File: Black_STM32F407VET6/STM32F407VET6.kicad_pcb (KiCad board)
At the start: 2 copper layers, 81.3 x 99.7 mm, 103 parts, among them J1 T0, J10 Fan2, J11 Fan1, J12 X_logic, J13 Microsteps, J14 X-, J15 Y-, J16 Z-, J17 Left, J18 Y_logic, J19 X+, J2 T1, J20 Y+, J21 Z+, J22 Microsteps, J23 EXP2, J24 Z_logic, J25 Bottom, J26 Microsteps, J27 EXP1, J28 E0_logic, J29 Microsteps, J3 TB, J30 Right, J31 E1_logic, J32 Microsteps, J33 X_motor, J34 Y_motor, J35 Z_motor, J36 E0_motor, J37 E1_motor, J38 X, J39 Y, J4 TC, J40 Z, J41 E0, J42 E1, J43 Fan0, J44 COM, J45 USB, J47 I2C, J48 SPI, J49 SPI, J5 + VIN -, J50 SDIO, J51 Servo, J52 Servo, J53 PowerSelect, J54 Power, J55 PD11, J56 Power, J6 - HotBed +, J7 Heater0, J8 Heater1, J9 Fan3, Q1 Q_NMOS_GDS, Q2 Q_NMOS_GDS, Q3 Q_NMOS_GDS, Q4 Q_NMOS_GSD, Q5 Q_NMOS_GSD, Q6 Q_NMOS_GSD, Q7 Q_NMOS_GSD, U1 SN74AHC, U2 SN74AHC, U3 SN74AHC, U4 LM2596S-5, U5 AT24CS01-SSHM

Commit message: Changed parts in schematic to be cheaper, PCB changed to be DIY friendly
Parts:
- removed REF**: OSHW-Symbol_6.7x6mm_SilkScreen, Symbol:OSHW-Symbol_6.7x6mm_SilkScreen
- removed U1, U2, U3: SN74AHC, Package_TO_SOT_SMD:SOT-23-5
- added Q10: BCX70, Package_TO_SOT_SMD:SOT-23, F.Cu at (217.6, 379.5)
- added Q11: BCX70, Package_TO_SOT_SMD:SOT-23, F.Cu at (214.1, 384.3)
- added Q12: IRLR8726PBF, Package_TO_SOT_SMD:TO-252-2, F.Cu at (227.9, 334.9)
- added Q13: IRLR8726PBF, Package_TO_SOT_SMD:TO-252-2, F.Cu at (213.0, 347.5)
- added Q14: IRLR8726PBF, Package_TO_SOT_SMD:TO-252-2, F.Cu at (200.0, 359.8)
- added Q8: IRLML0030TRPBF, Package_TO_SOT_SMD:SOT-23, F.Cu at (223.9, 375.0)
- added Q9: BCX70, Package_TO_SOT_SMD:SOT-23, F.Cu at (219.5, 375.0)
- added R23: 100K, Resistor_SMD:R_0603_1608Metric, F.Cu at (251.8, 344.4)
- added R24: 100K, Resistor_SMD:R_0603_1608Metric, F.Cu at (256.2, 339.9)
- added R25: 100K, Resistor_SMD:R_0603_1608Metric, F.Cu at (189.4, 384.4)
- added R26: 10K, Resistor_SMD:R_0603_1608Metric, F.Cu at (237.3, 365.2)
- added R27: 10K, Resistor_SMD:R_0603_1608Metric, F.Cu at (228.1, 374.8)
- added R28: 10K, Resistor_SMD:R_0603_1608Metric, F.Cu at (253.6, 349.4)
- D1, R18, R19, R20, R21, R22: moved to F.Cu
- J1, J2, J3, J4: footprint Connector_JST:JST_XH_B02B-XH-A_1x02_P2.50mm_Vertical -> Connector_JST:JST_XH_B2B-XH-AM_1x02_P2.50mm_Vertical
- J10: value Fan2 -> - HotBed +; footprint Connector_JST:JST_XH_B02B-XH-A_1x02_P2.50mm_Vertical -> Connector_JST:JST_XH_B2B-XH-A_1x02_P2.50mm_Vertical
- J11: value Fan1 -> Heater0; footprint Connector_JST:JST_XH_B02B-XH-A_1x02_P2.50mm_Vertical -> Connector_JST:JST_XH_B2B-XH-A_1x02_P2.50mm_Vertical
- J14, J15, J16, J19, J20, J21: footprint Connector_JST:JST_XH_B03B-XH-A_1x03_P2.50mm_Vertical -> Connector_JST:JST_XH_B3B-XH-A_1x03_P2.50mm_Vertical
- J38, J39, J40, J41, J42: footprint Connector_JST:JST_XH_B04B-XH-A_1x04_P2.50mm_Vertical -> Connector_JST:JST_XH_B4B-XH-A_1x04_P2.50mm_Vertical
- J43: value Fan0 -> Heater1; footprint Connector_JST:JST_XH_B02B-XH-A_1x02_P2.50mm_Vertical -> Connector_JST:JST_XH_B2B-XH-AM_1x02_P2.50mm_Vertical
- J50: footprint Connector_JST:JST_XH_B09B-XH-A_1x09_P2.50mm_Vertical -> Connector_JST:JST_XH_B9B-XH-A_1x09_P2.50mm_Vertical
- J6: value - HotBed + -> Fan3; footprint TerminalBlock_MetzConnect:TerminalBlock_MetzConnect_Type055_RT01502HDWU_1x02_P5.00mm_Horizontal -> Connector_JST:JST_XH_B2B-XH-AM_1x02_P2.50mm_Vertical
- J7: value Heater0 -> Fan2; footprint TerminalBlock_MetzConnect:TerminalBlock_MetzConnect_Type059_RT06302HBWC_1x02_P3.50mm_Horizontal -> Connector_JST:JST_XH_B2B-XH-AM_1x02_P2.50mm_Vertical
- J8: value Heater1 -> Fan1; footprint TerminalBlock_MetzConnect:TerminalBlock_MetzConnect_Type059_RT06302HBWC_1x02_P3.50mm_Horizontal -> Connector_JST:JST_XH_B2B-XH-AM_1x02_P2.50mm_Vertical
- J9: value Fan3 -> Fan0; footprint Connector_JST:JST_XH_B02B-XH-A_1x02_P2.50mm_Vertical -> Connector_JST:JST_XH_B2B-XH-AM_1x02_P2.50mm_Vertical
- Q1, Q2, Q3: value Q_NMOS_GDS -> BCX70; footprint Package_TO_SOT_SMD:TO-252-2 -> Package_TO_SOT_SMD:SOT-23
- Q4, Q6, Q7: value Q_NMOS_GSD -> IRLML0030TRPBF
- Q5: value Q_NMOS_GSD -> BCX70
- R10, R12, R14: value 10 -> 100K
- R13: value 10K -> 100K
- R16: value 10 -> 10K
- moved J24 336.8 mm to (113.0, 398.3)
- moved J26 328.3 mm to (106.2, 400.8)
- moved C11 313.9 mm to (171.7, 380.5), turned to 0 degrees
- moved J27 312.5 mm to (155.2, 458.5), turned to 0 degrees
- moved R7 311.8 mm to (147.8, 385.4), turned to 0 degrees
- moved R6 311.7 mm to (143.7, 385.4), turned to 0 degrees
- moved J47 309.9 mm to (216.4, 402.3)
- moved J4 308.2 mm to (239.8, 393.2), turned to 0 degrees
- moved C7 307.1 mm to (171.7, 370.6), turned to 0 degrees
- moved R9 306.9 mm to (221.9, 378.5), turned to 0 degrees
- moved R8 304.0 mm to (228.1, 372.3), turned to 0 degrees
- moved R1 296.0 mm to (151.8, 385.4), turned to 0 degrees
- moved R2 295.2 mm to (162.5, 384.3), turned to 0 degrees
- moved C4 294.0 mm to (211.2, 378.7)
- moved J3 293.3 mm to (273.8, 361.7), turned to 0 degrees
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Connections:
- J10 pad 1: Net-(J10-Pad1) -> 12V
- J11 pad 1: Net-(J10-Pad1) -> 12V
- J43 pad 1: Net-(J10-Pad1) -> 12V
- J56 pad 2: Net-(J10-Pad1) -> GND
- J7 pad 1: Net-(J7-Pad1) -> 12V
- J7 pad 2: 12V -> Net-(J7-Pad2)
- J8 pad 1: Net-(J8-Pad1) -> 12V
- J8 pad 2: 12V -> Net-(J8-Pad2)
- J9 pad 1: Net-(J10-Pad1) -> 12V
- Q1 pad 1: Net-(Q1-Pad1) -> GND
- Q1 pad 2: Net-(J6-Pad2) -> Net-(Q1-Pad2)
- Q1 pad 3: GND -> Net-(Q1-Pad3)
- Q2 pad 1: Net-(Q2-Pad1) -> GND
- Q2 pad 2: Net-(J7-Pad1) -> Net-(Q2-Pad2)
- Q2 pad 3: GND -> Net-(Q2-Pad3)
- Q3 pad 1: Net-(Q3-Pad1) -> GND
- Q3 pad 2: Net-(J8-Pad1) -> Net-(Q3-Pad2)
- Q3 pad 3: GND -> Net-(Q3-Pad3)
- Q4 pad 1: Net-(Q4-Pad1) -> Net-(Q3-Pad3)
- Q4 pad 3: Net-(J9-Pad2) -> Net-(J8-Pad2)
- Q5 pad 1: Net-(Q5-Pad1) -> GND
- Q5 pad 2: GND -> Net-(Q5-Pad2)
- Q5 pad 3: Net-(J10-Pad2) -> Net-(Q5-Pad3)
- Q6 pad 1: Net-(Q6-Pad1) -> Net-(Q1-Pad3)
- Q6 pad 3: Net-(J11-Pad2) -> Net-(J6-Pad2)
- Q7 pad 1: Net-(Q7-Pad1) -> Net-(Q2-Pad3)
- Q7 pad 3: Net-(J43-Pad2) -> Net-(J7-Pad2)
- R10 pad 1: Net-(Q4-Pad1) -> Fan3
- R10 pad 2: Fan3 -> Net-(Q1-Pad2)
- R11 pad 1: GND -> Net-(Q3-Pad3)
- R11 pad 2: Net-(Q4-Pad1) -> 12V
- R12 pad 1: Net-(Q5-Pad1) -> Fan2
- R12 pad 2: Fan2 -> Net-(Q2-Pad2)
- R13 pad 1: GND -> Fan1
- R13 pad 2: Net-(Q5-Pad1) -> Net-(Q3-Pad2)
- R14 pad 1: Net-(Q6-Pad1) -> Fan0
- R14 pad 2: Fan1 -> Net-(Q5-Pad2)
- R15 pad 1: GND -> Net-(Q1-Pad3)
- R15 pad 2: Net-(Q6-Pad1) -> 12V
- R16 pad 1: Net-(Q7-Pad1) -> Net-(Q2-Pad3)
- R16 pad 2: Fan0 -> 12V
- R17 pad 1: GND -> Net-(Q5-Pad3)
- R17 pad 2: Net-(Q7-Pad1) -> 12V
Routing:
- net GND: track 756.5 -> 0.00 mm, vias 104 -> 0
- net 5V: track 268.4 -> 0.00 mm, vias 1 -> 0
- net 3V3: track 325.5 -> 66.4 mm, vias 5 -> 0
- net 12V: track 304.2 -> 73.4 mm, vias 5 -> 0
- net Z_En: track 79.3 -> 0.00 mm, vias 1 -> 0
- net X_En: track 69.6 -> 0.00 mm
- net Y-: track 67.5 -> 0.00 mm
- net Heater0: track 63.9 -> 0.00 mm
- net Z_Step: track 62.3 -> 0.00 mm
- net Z_Dir: track 62.3 -> 0.00 mm
- net E0_En: track 57.1 -> 0.00 mm
- net Heater1: track 53.7 -> 0.00 mm
- net Y_En: track 53.0 -> 0.00 mm, vias 1 -> 0
- net E1_En: track 51.2 -> 0.00 mm, vias 1 -> 0
- net Y+: track 51.1 -> 0.00 mm
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- removed copper zone on B.Cu, net GND
- removed copper zone on F.Cu, net GND
- removed copper zone on B.Cu, net Net-(J6-Pad2)
- removed copper zone on B.Cu, net Net-(J7-Pad1)
- removed copper zone on B.Cu, net Net-(J8-Pad1)
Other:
- board outline removed
- rule pad_to_mask_clearance: 0.051 -> 0
- board text removed: "3V3"
- board text removed: "5V"
- board text removed: "CLK"
- board text removed: "CMD"
- board text removed: "CS"
- board text removed: "CS1"
- board text removed: "CS2"
- board text removed: "D0"
- board text removed: "D1"
- board text removed: "D2"
- board text removed: "D3"
- board text removed: "DM"
- board text removed: "DP"
- board text removed: "Gnd"
- board text removed: "MISO"
- board text removed: "MOSI"
- board text removed: "PWM"
- board text removed: "Rx"
- board text removed: "SCK"
- board text removed: "SCL"
- board text removed: "SDA"
- board text removed: "SDDET"
- board text removed: "T0"
- board text removed: "T1"
- board text removed: "TB"
- board text removed: "TC"
- board text removed: "Tx"
- board text removed: "VIN"
- board text removed: "Vcc"
- board text removed: "X+"
- board text removed: "X-"
- board text removed: "Y+"
- board text removed: "Y-"
- board text removed: "Z+"
- board text removed: "Z-"
- board text removed: "https://github.com/jmz52/hardware"

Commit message: Arranged parts on PCB, swapped a few pins in schematic to align connectors.
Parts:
- removed C11: 100uF 35V, Capacitor_SMD:CP_Elec_8x6.9
- removed C5: 100uF 35V, Capacitor_THT:CP_Radial_D8.0mm_P3.50mm
- removed C6: 220uF 35V, Capacitor_THT:CP_Radial_D6.3mm_P2.50mm
- removed D1: SS14, Diode_SMD:D_SMA
- removed J21: Z+, Connector_JST:JST_XH_B3B-XH-A_1x03_P2.50mm_Vertical
- removed J31: E1_logic, Connector_PinSocket_2.54mm:PinSocket_1x08_P2.54mm_Vertical
- removed J32: Microsteps, Connector_PinHeader_2.54mm:PinHeader_2x03_P2.54mm_Vertical
- removed J35: Z_motor, Connector_PinSocket_2.54mm:PinSocket_1x08_P2.54mm_Vertical
- removed J37: E1_motor, Connector_PinSocket_2.54mm:PinSocket_1x08_P2.54mm_Vertical
- removed J40: Z, Connector_JST:JST_XH_B4B-XH-A_1x04_P2.50mm_Vertical
- removed J42: E1, Connector_JST:JST_XH_B4B-XH-A_1x04_P2.50mm_Vertical
- removed J45: USB, Connector_PinHeader_2.54mm:PinHeader_1x04_P2.54mm_Vertical
- removed L1: 47uH, Inductor_THT:L_Radial_D9.5mm_P5.00mm_Fastron_07HVP
- removed R6, R7, R8, R9: 4K7, Resistor_SMD:R_0603_1608Metric
- removed U4: LM2596S-5, Package_TO_SOT_SMD:TO-263-5_TabPin3
- added JXXX1: ESC_POWER, TerminalBlock_MetzConnect:TerminalBlock_MetzConnect_Type055_RT01502HDWU_1x02_P5.00mm_Horizontal, F.Cu at (144.8, 118.7)
- J12: value X_logic -> X-; footprint Connector_PinSocket_2.54mm:PinSocket_1x08_P2.54mm_Vertical -> Connector_JST:JST_XH_B3B-XH-A_1x03_P2.50mm_Vertical
- J13: value Microsteps -> Y-; footprint Connector_PinHeader_2.54mm:PinHeader_2x03_P2.54mm_Vertical -> Connector_JST:JST_XH_B3B-XH-A_1x03_P2.50mm_Vertical
- J14: value X- -> Z-
- J15: value Y- -> Z+
- J16: value Z- -> USB_B; footprint Connector_JST:JST_XH_B3B-XH-A_1x03_P2.50mm_Vertical -> Connector_USB:USB_B_OST_USB-B1HSxx_Horizontal
- J17: value Left -> X_logic; footprint Connector_PinSocket_2.54mm:PinSocket_2x24_P2.54mm_Vertical -> Connector_PinSocket_2.54mm:PinSocket_1x08_P2.54mm_Vertical; moved to F.Cu
- J19: value X+ -> Z_logic; footprint Connector_JST:JST_XH_B3B-XH-A_1x03_P2.50mm_Vertical -> Connector_PinSocket_2.54mm:PinSocket_1x08_P2.54mm_Vertical
- J20: value Y+ -> E0_logic; footprint Connector_JST:JST_XH_B3B-XH-A_1x03_P2.50mm_Vertical -> Connector_PinSocket_2.54mm:PinSocket_1x08_P2.54mm_Vertical
- J22: value Microsteps -> Left; footprint Connector_PinHeader_2.54mm:PinHeader_2x03_P2.54mm_Vertical -> Connector_PinSocket_2.54mm:PinSocket_2x24_P2.54mm_Vertical; moved to B.Cu
- J24: value Z_logic -> LCD2004; footprint Connector_PinSocket_2.54mm:PinSocket_1x08_P2.54mm_Vertical -> Connector_JST:JST_XH_B10B-XH-A_1x10_P2.50mm_Vertical
- J26: value Microsteps -> Right; footprint Connector_PinHeader_2.54mm:PinHeader_2x03_P2.54mm_Vertical -> Connector_PinSocket_2.54mm:PinSocket_2x24_P2.54mm_Vertical; moved to B.Cu
- J27: value EXP1 -> Z_motor; footprint Connector_IDC:IDC-Header_2x05_P2.54mm_Vertical -> Connector_PinSocket_2.54mm:PinSocket_1x08_P2.54mm_Vertical
- J28: value E0_logic -> LIGHTS; footprint Connector_PinSocket_2.54mm:PinSocket_1x08_P2.54mm_Vertical -> Connector_JST:JST_XH_B3B-XH-A_1x03_P2.50mm_Vertical
- J29: value Microsteps -> Z; footprint Connector_PinHeader_2.54mm:PinHeader_2x03_P2.54mm_Vertical -> Connector_JST:JST_XH_B4B-XH-A_1x04_P2.50mm_Vertical
- J30: value Right -> Z; footprint Connector_PinSocket_2.54mm:PinSocket_2x24_P2.54mm_Vertical -> Connector_JST:JST_XH_B4B-XH-A_1x04_P2.50mm_Vertical; moved to F.Cu
- Q12, Q13, Q14, Q3, Q4, R11, R13, R18, R19: moved to B.Cu
- R5: value 4K7 -> 1,5k; moved to B.Cu
- moved J53 427.5 mm to (27.7, 42.9)
- moved J4 390.1 mm to (52.3, 51.1)
- moved J3 387.3 mm to (52.3, 43.9)
- moved J52 385.4 mm to (51.1, 33.8)
- moved J51 381.7 mm to (54.9, 33.8)
- moved J54 372.9 mm to (24.0, 43.0)
- moved J27 368.7 mm to (45.7, 106.4), turned to 180 degrees
- moved R1 363.7 mm to (259.8, 38.1)
- moved R2 361.1 mm to (259.8, 36.6)
- moved C4 333.6 mm to (258.9, 48.5)
- moved U5 333.6 mm to (260.8, 42.0)
- moved J26 327.4 mm to (188.0, 83.8), turned to 180 degrees
- moved R20 318.1 mm to (263.1, 38.2)
- moved R21 316.2 mm to (263.1, 36.6)
- moved C2 315.5 mm to (266.4, 47.0), turned to 270 degrees
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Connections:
- J12 pad 1: X_En -> X-
- J12 pad 2: Net-(J12-Pad2) -> GND
- J12 pad 3: Net-(J12-Pad3) -> 5V
- J13 pad 1: Net-(J12-Pad2) -> Y-
- J13 pad 2: 3V3 -> GND
- J13 pad 3: Net-(J12-Pad3) -> 5V
- J14 pad 1: X- -> Z-
- J15 pad 1: Y- -> Z+
- J16 pad 1: Z- -> 5V
- J16 pad 2: GND -> Net-(J16-Pad2)
- J16 pad 3: 5V -> Net-(J16-Pad3)
- J17 pad 1: 5V -> X_En
- J17 pad 2: 5V -> Tmc_MOSI
- J17 pad 3: 5V -> Tmc_SCK
- J17 pad 4: 5V -> X_CS
- J17 pad 5: 3V3 -> Tmc_MISO
- J17 pad 6: 3V3 -> Net-(J17-Pad6)
- J17 pad 7: 3V3 -> X_Step
- J17 pad 8: 3V3 -> X_Dir
- J18 pad 2: Net-(J18-Pad2) -> Tmc_MOSI
- J18 pad 3: Net-(J18-Pad3) -> Tmc_SCK
- J18 pad 4: Net-(J18-Pad4) -> Y_Step
- J18 pad 5: Net-(J18-Pad5) -> Tmc_MISO
- J18 pad 6: Net-(J18-Pad5) -> Net-(J18-Pad6)
- J18 pad 7: Y_Step -> Y_CS
- J19 pad 1: X+ -> Z_En
- J19 pad 2: GND -> Tmc_MOSI
- J19 pad 3: 5V -> Tmc_SCK
- J20 pad 1: Y+ -> E0_En
- J20 pad 2: GND -> Tmc_MOSI
- J20 pad 3: 5V -> Tmc_SCK
- J22 pad 1: Net-(J18-Pad2) -> 5V
- J22 pad 2: 3V3 -> 5V
- J22 pad 3: Net-(J18-Pad3) -> 5V
- J22 pad 4: 3V3 -> 5V
- J22 pad 5: Net-(J18-Pad4) -> 3V3
- J24 pad 1: Z_En -> GND
- J24 pad 2: Net-(J24-Pad2) -> 5V
- J24 pad 3: Net-(J24-Pad3) -> 3V3
- J24 pad 4: Net-(J24-Pad4) -> LCD4
- J24 pad 5: Net-(J24-Pad5) -> LCDRS
- J24 pad 6: Net-(J24-Pad5) -> LCD5
- J24 pad 7: Z_Step -> LCDE
- J24 pad 8: Z_Dir -> LCD6
- J25 pad 11: LCD4 -> LCDE
- J25 pad 13: LCD7 -> LCD6
- J25 pad 15: LCD6 -> LCD7
- J25 pad 5: LCDE -> LCD4
- J25 pad 6: LCDRS -> Fan3
- J25 pad 7: Fan3 -> LCDRS
- J26 pad 1: Net-(J24-Pad2) -> 3V3
- J26 pad 3: Net-(J24-Pad3) -> 3V3
- J26 pad 5: Net-(J24-Pad4) -> GND
- J26 pad 6: 3V3 -> Net-(J26-Pad6)
- J27 pad 1: 5V -> 12V
- J27 pad 3: LCD7 -> Net-(J27-Pad3)
- J27 pad 4: LCD6 -> Net-(J27-Pad4)
- J27 pad 5: LCD5 -> Net-(J27-Pad5)
- J27 pad 6: LCD4 -> Net-(J27-Pad6)
- J27 pad 7: LCDRS -> 3V3
- J27 pad 8: LCDE -> GND
- J28 pad 1: E0_En -> 5V
- J28 pad 2: Net-(J28-Pad2) -> LIGHT_DIN
- J28 pad 3: Net-(J28-Pad3) -> GND
- J29 pad 1: Net-(J28-Pad2) -> Net-(J27-Pad3)
- J29 pad 2: 3V3 -> Net-(J27-Pad4)
- J29 pad 3: Net-(J28-Pad3) -> Net-(J27-Pad5)
- J29 pad 4: 3V3 -> Net-(J27-Pad6)
- J30 pad 1: 3V3 -> Net-(J27-Pad3)
- J30 pad 2: 3V3 -> Net-(J27-Pad4)
- J30 pad 3: 3V3 -> Net-(J27-Pad5)
- J30 pad 4: 3V3 -> Net-(J27-Pad6)
- J50 pad 1: SDIO_D0 -> GND
- J50 pad 2: SDIO_DET -> 3V3
- J50 pad 3: SDIO_D1 -> SDIO_D0
- J50 pad 4: SDIO_CMD -> SDIO_D1
- J50 pad 5: SDIO_SCK -> SDIO_DET
- J50 pad 6: GND -> SDIO_D2
- J50 pad 8: 3V3 -> SDIO_SCK
- J50 pad 9: SDIO_D2 -> SDIO_CMD
- R18 pad 2: Net-(J45-Pad2) -> Net-(J16-Pad2)
- R19 pad 2: Net-(J45-Pad3) -> Net-(J16-Pad3)
- R5 pad 1: GND -> Net-(J16-Pad3)
- R5 pad 2: Net-(J12-Pad2) -> 5V
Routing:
- net MISO: track 0.00 -> 63.5 mm
- net CLK: track 0.00 -> 44.3 mm
- net MOSI: track 0.00 -> 40.3 mm
- net 5V: track 0.00 -> 36.8 mm
- net Tmc_MISO: track 0.00 -> 35.2 mm
- net 12V: track 73.4 -> 102.5 mm
- net GND: track 0.00 -> 22.6 mm
- net Net-(J37-Pad6): track 18.7 -> 0.00 mm
- net Net-(J35-Pad6): track 18.3 -> 0.00 mm
- net Tmc_MOSI: track 0.00 -> 17.3 mm
- net Tmc_SCK: track 0.00 -> 17.3 mm
- net Fan1: track 0.00 -> 16.6 mm
- net RX: track 0.00 -> 14.9 mm
- net Net-(J37-Pad5): track 14.8 -> 0.00 mm
- net Net-(J35-Pad5): track 14.7 -> 0.00 mm
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
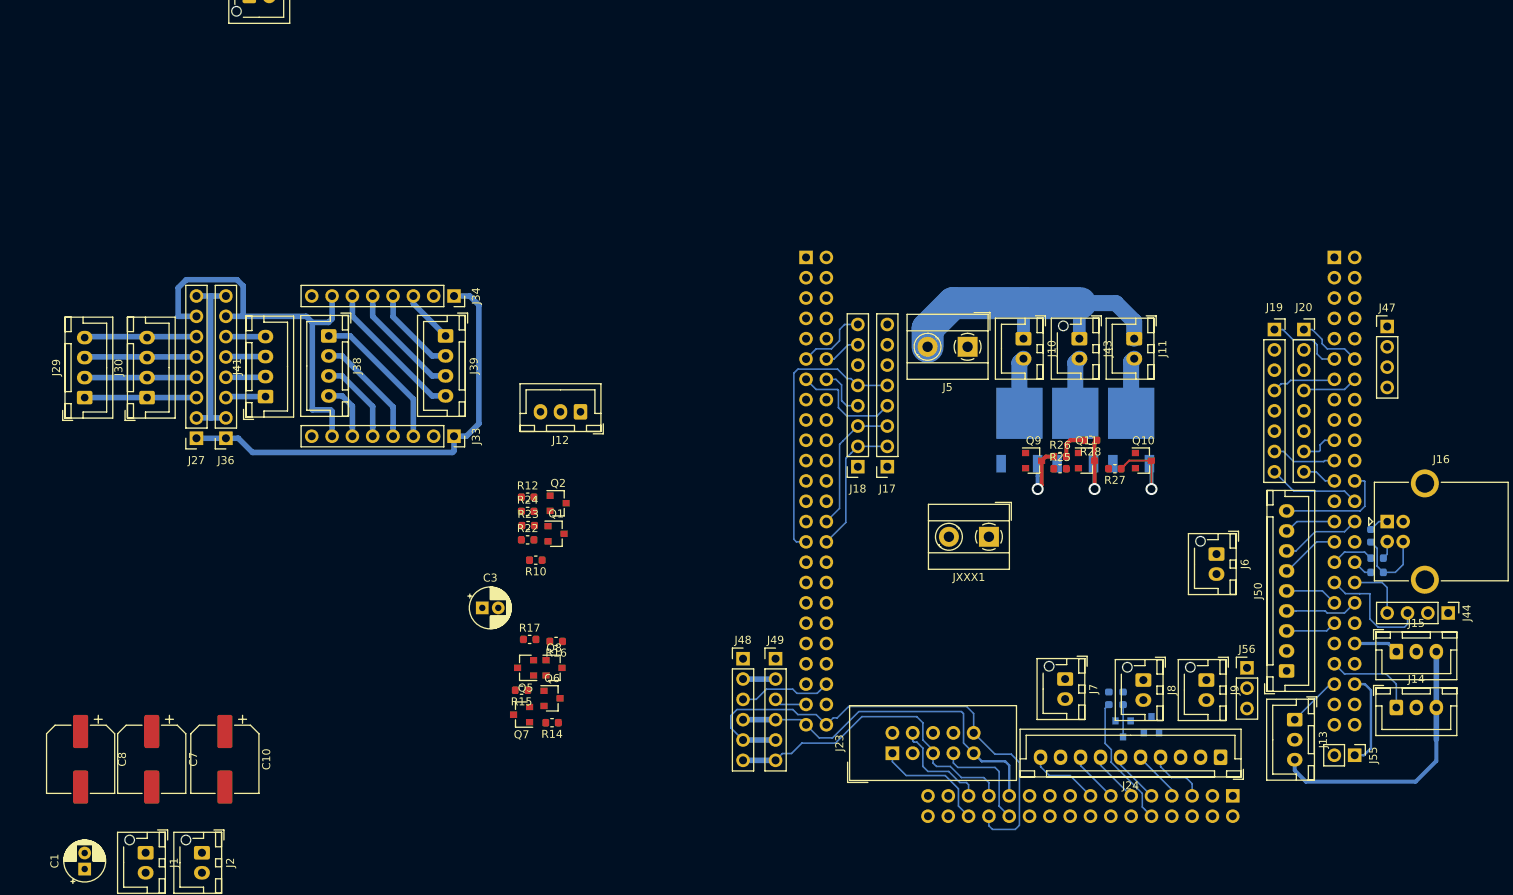
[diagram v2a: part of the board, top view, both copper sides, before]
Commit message: Flash button, Endstops, Drivers moved
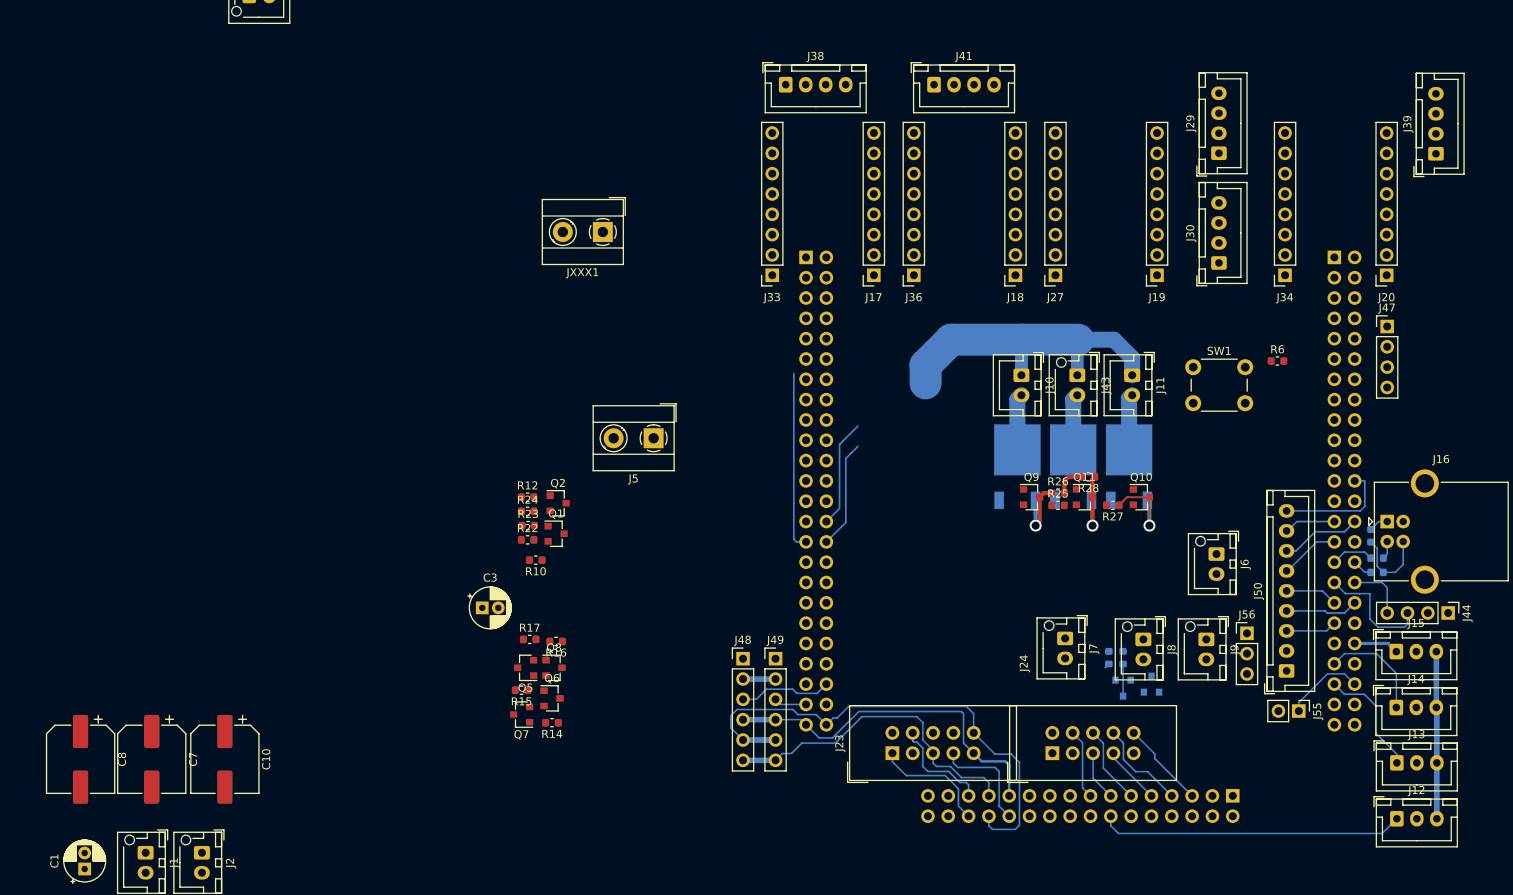
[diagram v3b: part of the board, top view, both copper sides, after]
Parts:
- added R6: R4.7K, Resistor_SMD:R_0603_1608Metric, F.Cu at (180.8, 96.8)
- added SW1: Boot0, Button_Switch_THT:SW_PUSH_6mm_H5mm, F.Cu at (170.3, 97.5)
- J24: footprint Connector_JST:JST_XH_B10B-XH-A_1x10_P2.50mm_Vertical -> Connector_IDC:IDC-Header_2x05_P2.54mm_Vertical
- moved J29 145.0 mm to (173.5, 70.8)
- moved J30 135.0 mm to (173.5, 84.5)
- moved J39 125.9 mm to (200.7, 70.9), turned to 90 degrees
- moved J12 114.0 mm to (195.8, 154.0), turned to 0 degrees
- moved J27 109.3 mm to (153.1, 86.1)
- moved J34 103.9 mm to (181.8, 86.1), turned to 180 degrees
- moved J41 92.2 mm to (137.9, 62.2), turned to 0 degrees
- moved J36 88.4 mm to (135.4, 86.1)
- moved J38 65.2 mm to (119.4, 62.2), turned to 0 degrees
- moved JXXX1 61.5 mm to (96.5, 80.6)
- moved J33 44.6 mm to (117.7, 86.1), turned to 180 degrees
- moved J5 40.9 mm to (102.9, 106.4)
- moved J18 31.0 mm to (148.1, 86.1)
- moved J17 24.0 mm to (130.4, 86.1)
- moved J24 21.0 mm to (152.7, 145.8), turned to 90 degrees
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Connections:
- J22 pad 11: Y_Dir -> X_Step
- J22 pad 15: Y_En -> X_En
- J22 pad 16: X- -> Y_Dir
- J22 pad 31: X_Step -> X_Dir
- J22 pad 35: X_En -> Net-(J22-Pad35)
- J25 pad 11: LCDE -> LCD5
- J25 pad 13: LCD6 -> LCDRS
- J25 pad 14: Net-(J25-Pad14) -> X-
- J25 pad 15: LCD7 -> LCD4
- J25 pad 5: LCD4 -> LCD7
- J25 pad 7: LCDRS -> LCD6
- J25 pad 9: LCD5 -> LCDE
- J26 pad 20: X_Dir -> Y_En
- J26 pad 5: GND -> Net-(J26-Pad5)
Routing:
- net 12V: track 102.5 -> 45.5 mm
- net 3V3: track 55.8 -> 4.06 mm
- net X-: track 0.00 -> 38.1 mm
- net GND: track 22.6 -> 0.00 mm
- net Net-(J33-Pad3): track 18.5 -> 0.00 mm
- net Net-(J34-Pad6): track 18.3 -> 0.00 mm
- net Fan1: track 16.6 -> 0.65 mm
- net Net-(J34-Pad5): track 14.7 -> 0.00 mm
- net Net-(J33-Pad4): track 14.3 -> 0.00 mm
- net Net-(J27-Pad6): track 14.0 -> 0.00 mm
- net Net-(J27-Pad5): track 14.0 -> 0.00 mm
- net Net-(J27-Pad4): track 14.0 -> 0.00 mm
- net Net-(J27-Pad3): track 14.0 -> 0.00 mm
- net X_CS: track 13.8 -> 0.00 mm
- net 5V: track 36.8 -> 23.4 mm
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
